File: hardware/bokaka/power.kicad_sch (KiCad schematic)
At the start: 5 parts, among them U1 AP2112K-3.3

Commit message: Adding rest of design and pdf
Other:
- moved on the sheet: BT1, C1, C2, R1, U1

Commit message: Finalize design before pcb
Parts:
- removed BT1: CR2032 Battery, Footprints:BAT-TH_CR2032-BS-6-1, symbol Device:Battery_Cell
- removed C2: 10u, symbol Device:C
- removed R1: 10k, symbol Device:R
- removed U1: AP2112K-3.3, Package_TO_SOT_SMD:SOT-23-5, symbol Regulator_Linear:AP2112K-3.3
- added BT2: CR2450 Battery, Battery:BatteryHolder_Keystone_3009_1x2450, symbol Device:Battery_Cell
- added C15, C17, C19, C21: 10u, Capacitor_SMD:C_0402_1005Metric, symbol Device:C
- added C16, C18, C20: 0.1u, Capacitor_SMD:C_0402_1005Metric, symbol Device:C
- added L1: 2.2uH, Inductor_SMD:L_0603_1608Metric, symbol Device:L
- added R10: 100k, Resistor_SMD:R_0402_1005Metric, symbol Device:R
- added R11: 36.5k, Resistor_SMD:R_0402_1005Metric, symbol Device:R
- added R12: 0, Resistor_SMD:R_0402_1005Metric, symbol Device:R
- added R13: 16.2k, Resistor_SMD:R_0402_1005Metric, symbol Device:R
- added R8: 1M, Resistor_SMD:R_0402_1005Metric, symbol Device:R
- added R9: 820k, Resistor_SMD:R_0402_1005Metric, symbol Device:R
- added TP1, TP2: TestPoint, symbol Connector:TestPoint
- added U5: TPS63900, Package_SON:WSON-10-1EP_2.5x2.5mm_P0.5mm_EP1.2x2mm_ThermalVias, symbol Regulator_Switching:TPS63900
- added U6: TPS2116DRL, Package_TO_SOT_SMD:SOT-583-8, symbol Power_Management:TPS2116DRL
- C1: value 10u -> 22u; footprint (none) -> Capacitor_SMD:C_0402_1005Metric
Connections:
- net +3V3: now also U5.6 (VOUT)
- net GND: now also BT2.2 (-), C15.2, C16.2, C17.2, C18.2, C19.2, C20.2, C21.2, R11.1, R12.1, R13.1, R9.2, U5.11 (GND), U5.8 (GND), U6.1 (GND)
- net VBUS renamed VSYS
- net VSYS: now also C15.1, C16.1, C21.1, R10.2, TP1.1, U5.1 (EN), U5.10 (VIN), U5.2 (SEL), U6.2 (VOUT), U6.7 (VOUT)
- new net: R8.2, R9.1, U6.4 (PR1)
- new net: L1.1, U5.9 (LX1)
- new net: L1.2, U5.7 (LX2)
- new net: R13.2, U5.5 (CFG3)
- new net: R11.2, U5.3 (CFG1)
- new net: R12.2, U5.4 (CFG2)
- new net +5V: BT2.1 (+), C17.1, C18.1, C19.1, C20.1, R8.1, U6.3 (VIN1), U6.5 (MODE), U6.6 (VIN2)
- new net USB_DETECT: R10.1, TP2.1, U6.8 (ST)

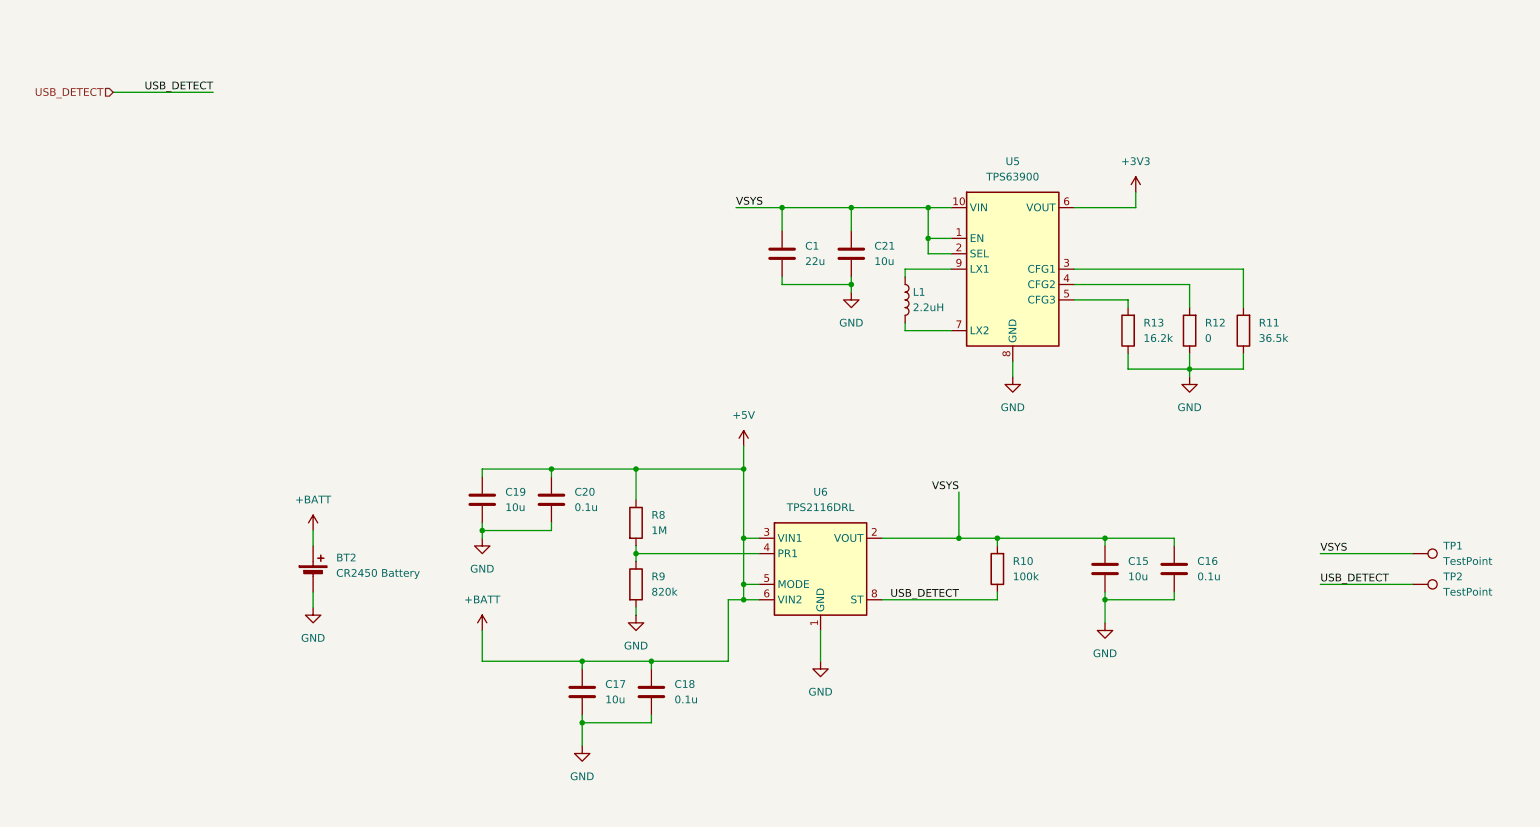
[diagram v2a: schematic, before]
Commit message: footprint asignment
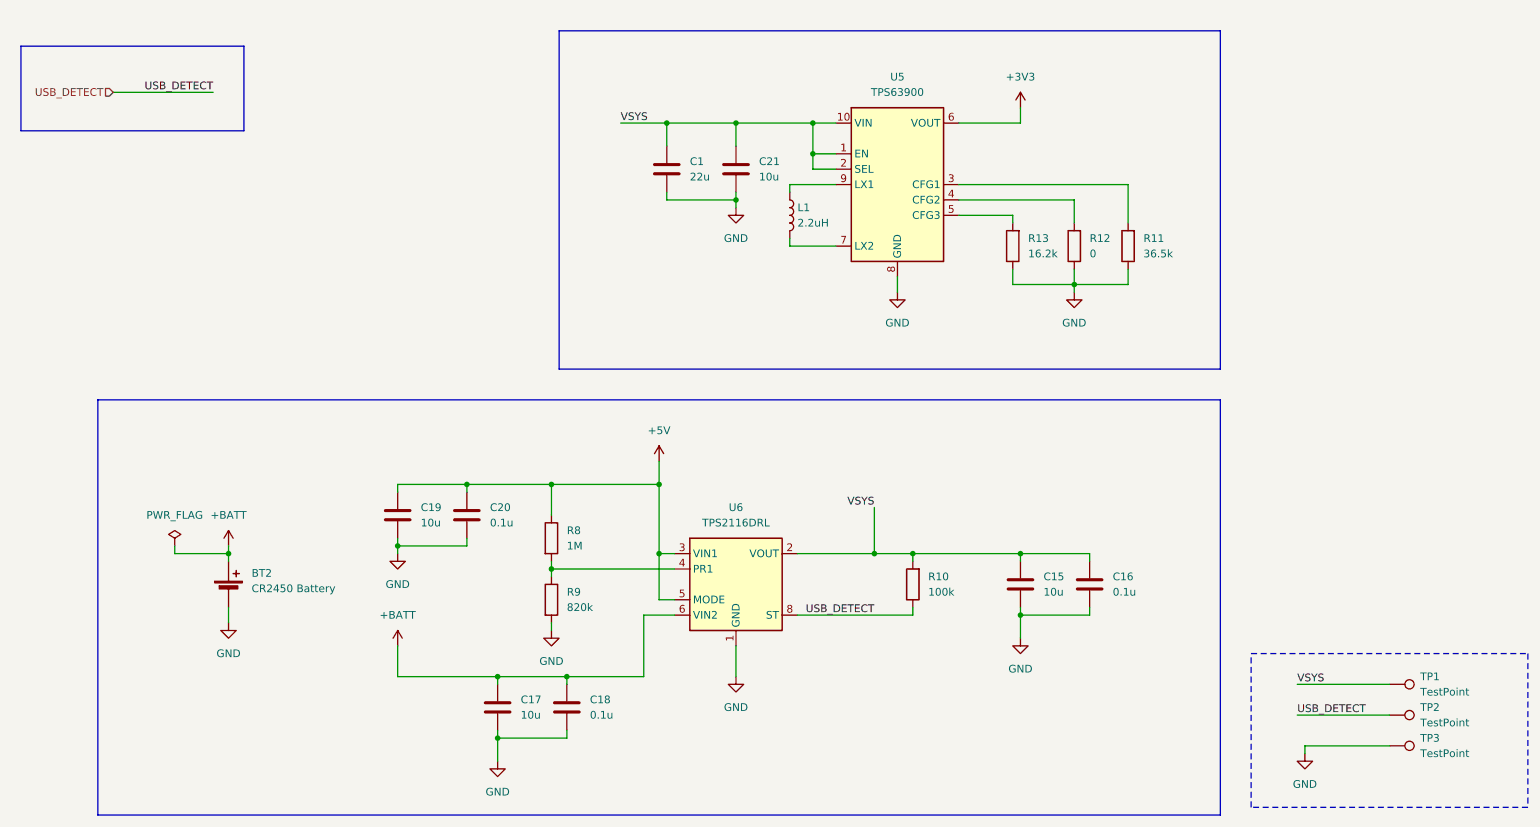
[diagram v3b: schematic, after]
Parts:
- added TP3: TestPoint, Connector_PinSocket_2.54mm:PinSocket_1x01_P2.54mm_Vertical, symbol Connector:TestPoint
- TP1: footprint (none) -> Connector_PinHeader_2.54mm:PinHeader_1x01_P2.54mm_Vertical
- TP2: footprint (none) -> Connector_PinSocket_2.54mm:PinSocket_1x01_P2.54mm_Vertical
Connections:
- net +5V: no longer BT2.1 (+), C17.1, C18.1, U6.6 (VIN2)
- net GND: now also TP3.1
- new net +BATT: BT2.1 (+), C17.1, C18.1, U6.6 (VIN2)
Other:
- moved on the sheet: BT2, C1, C15, C16, C17, C18, C19, C20, C21, L1, R10, R11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

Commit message: schematic update
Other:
- note added: "Buck boost"
- note added: "Power switching"
- note added: "Test points"
- note added: "interface"
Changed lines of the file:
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@@
 		(stroke
 			(width 0)
-			(type default)
+			(type dash)
 		)
 		(fill
@@
 		)
 	)
+	(text "Power switching"
+		(exclude_from_sim no)
+		(at 41.91 92.456 0)
+		(effects
+			(font
+				(size 1.27 1.27)
+			)
+		)
+	)
+	(text "interface"
+		(exclude_from_sim no)
+		(at 25.654 34.036 0)
+		(effects
+			(font
+				(size 1.27 1.27)
+			)
+		)
+	)
+	(text "Test points"
+		(exclude_from_sim no)
+		(at 229.87 134.366 0)
+		(effects
+			(font
+				(size 1.27 1.27)
+			)
+		)
+	)
+	(text "Buck boost"
+		(exclude_from_sim no)
+		(at 115.57 31.496 0)
+		(effects
+			(font
+				(size 1.27 1.27)
+			)
+		)
+	)

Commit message: hardware update
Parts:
- added TP4, TP5: TestPoint, Connector_PinHeader_2.54mm:PinHeader_1x01_P2.54mm_Vertical, symbol Connector:TestPoint
- C1: footprint Capacitor_SMD:C_0402_1005Metric -> Capacitor_SMD:C_0805_2012Metric
- C15, C17, C21: footprint Capacitor_SMD:C_0402_1005Metric -> Capacitor_SMD:C_0603_1608Metric
- C16, C18, C20: value 0.1u -> 100n
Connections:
- net +3V3: now also TP4.1
- net +BATT: now also TP5.1
